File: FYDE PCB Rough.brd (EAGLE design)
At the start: 99 x 65.7 mm, 4 parts, among them P1 SEN-11574, U1 MCU-MCP3008-I/P(DIP16-7.62MM), X1 RASPI_BOARD_B+_FP

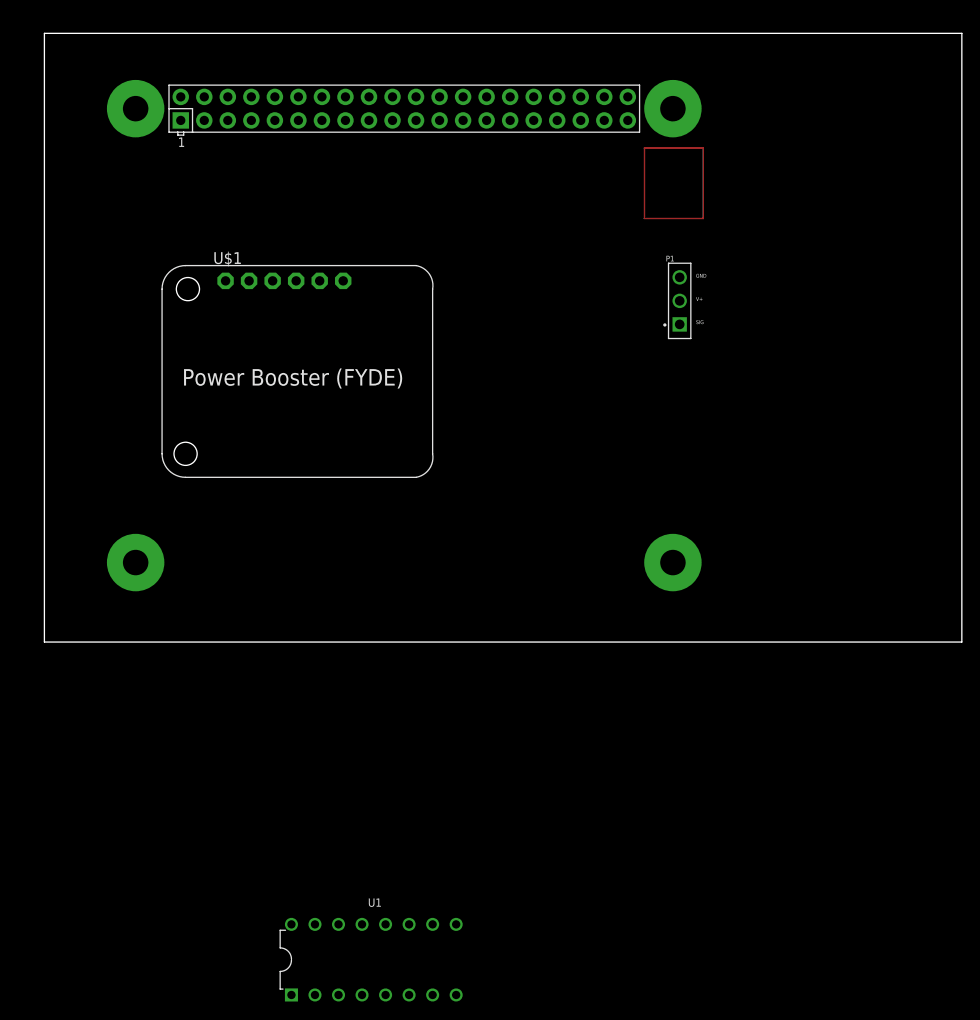
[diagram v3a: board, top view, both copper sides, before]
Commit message: schematic missing extra holes
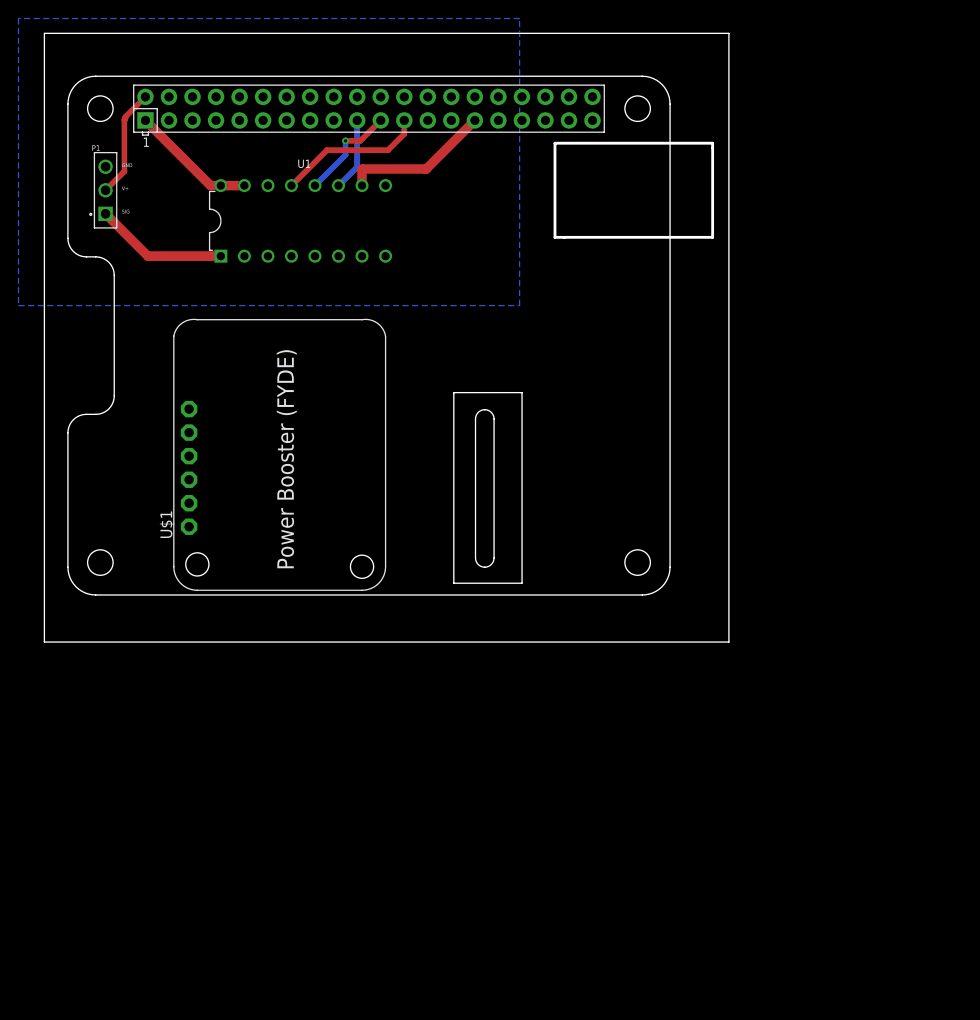
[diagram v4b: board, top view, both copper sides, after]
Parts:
- X1: value RASPI_BOARD_B+_FP -> RASPI_BOARD_B+_HDC; device raspberrypi_bastelstube_v13:RASPI_BOARD_B+_FULL_PAD -> raspberrypi_bastelstube_v13:RASPI_BOARD_B+HAT_DF_CF
- moved U1 80.1 mm to (27.9, 45.5)
- moved P1 63.1 mm to (6.60, 48.8)
- moved U$1 27.0 mm to (36.8, 5.59), turned to 90 degrees
- moved X1 3.81 mm to (2.54, 5.08)
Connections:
- removed net 3V3: X1.1
- removed net 5V0: X1.2
- removed net V+: P1.2
- new net +3V3A: U1.15, U1.16, X1.1
- new net +5V: P1.2, X1.2
- new net CLK: U1.13, X1.23
- new net CS: U1.10, X1.29
- new net MISO: U1.12, X1.21
- new net MOSI: U1.11, X1.19
- new net SIGNAL: P1.1, U1.1
- net GND: now also U1.14, U1.9
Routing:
- net N$7: track 27.9 -> 0.00 mm
- net CS: track 0.00 -> 16.1 mm
- net CLK: track 0.00 -> 15.9 mm
- net SIGNAL: track 0.00 -> 14.3 mm
- net +3V3A: track 0.00 -> 13.6 mm
- net +5V: track 0.00 -> 11.9 mm
- net MISO: track 0.00 -> 10.9 mm, vias 0 -> 1
- net MOSI: track 0.00 -> 7.87 mm
- added copper zone on layer 16, net GND
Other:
- board size 99 x 65.7 mm -> 73.9 x 65.7 mm
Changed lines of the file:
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@@
 <setting verticaltext="up"/>
 </settings>
-<grid distance="50" unitdist="mil" unit="mil" style="lines" multiple="1" display="no" altdistance="5" altunitdist="mil" altunit="mil"/>
+<grid distance="10" unitdist="mil" unit="mil" style="lines" multiple="1" display="no" altdistance="5" altunitdist="mil" altunit="mil"/>
 <layers>
 <layer number="1" name="Top" color="4" fill="1" visible="yes" active="yes"/>
@@
 <layer number="43" name="vRestrict" color="2" fill="10" visible="yes" active="yes"/>
 <layer number="44" name="Drills" color="7" fill="1" visible="no" active="yes"/>
-<layer number="45" name="Holes" color="7" fill="1" visible="no" active="yes"/>
+<layer number="45" name="Holes" color="7" fill="1" visible="yes" active="yes"/>
 <layer number="46" name="Milling" color="3" fill="1" visible="no" active="yes"/>
 <layer number="47" name="Measures" color="7" fill="1" visible="no" active="yes"/>
@@
 <board>
 <plain>
-<wire x1="0" y1="0" x2="99.04" y2="0" width="0" layer="20"/>
-<wire x1="99.04" y1="0" x2="99.04" y2="65.71" width="0" layer="20"/>
-<wire x1="99.04" y1="65.71" x2="0" y2="65.71" width="0" layer="20"/>
+<wire x1="0" y1="0" x2="73.894" y2="0" width="0" layer="20"/>
+<wire x1="73.894" y1="0" x2="73.894" y2="65.71" width="0" layer="20"/>
+<wire x1="73.894" y1="65.71" x2="0" y2="65.71" width="0" layer="20"/>
 <wire x1="0" y1="65.71" x2="0" y2="0" width="0" layer="20"/>
 <dimension x1="-16.129" y1="-139.7" x2="-9.906" y2="-116.967" x3="-29.083" y3="-128.3335" textsize="1.778" layer="47" dtype="vertical" unit="inch"/>
+<polygon width="0.3048" layer="20">
+<vertex x="55.118" y="53.848"/>
+<vertex x="72.136" y="53.848"/>
+<vertex x="72.136" y="53.34"/>
+<vertex x="72.136" y="43.688"/>
+<vertex x="56.134" y="43.688"/>
+<vertex x="55.118" y="43.688"/>
+</polygon>
+<rectangle x1="44.196" y1="6.35" x2="51.562" y2="26.924" layer="20"/>
 </plain>
 <attributes>
@@
 </autorouter>
 <elements>
-<element name="P1" library="SEN-11574" package="XDCR_SEN-11574" value="SEN-11574" x="68.58" y="36.83">
-<attribute name="AVAILABILITY" value="Unavailable" x="68.58" y="36.83" size="1.778" layer="27" display="off"/>
-<attribute name="DESCRIPTION" value=" PULSE SENSOR FOR ARDUINO " x="68.58" y="36.83" size="1.778" layer="27" display="off"/>
-<attribute name="MF" value="SparkFun" x="68.58" y="36.83" size="1.778" layer="27" display="off"/>
-<attribute name="MP" value="SEN-11574" x="68.58" y="36.83" size="1.778" layer="27" display="off"/>
-<attribute name="PACKAGE" value="None" x="68.58" y="36.83" size="1.778" layer="27" display="off"/>
-<attribute name="PRICE" value="None" x="68.58" y="36.83" size="1.778" layer="27" display="off"/>
+<element name="P1" library="SEN-11574" package="XDCR_SEN-11574" value="SEN-11574" x="6.604" y="48.768">
+<attribute name="AVAILABILITY" value="Unavailable" x="6.604" y="48.768" size="1.778" layer="27" display="off"/>
+<attribute name="DESCRIPTION" value=" PULSE SENSOR FOR ARDUINO " x="6.604" y="48.768" size="1.778" layer="27" display="off"/>
+<attribute name="MF" value="SparkFun" x="6.604" y="48.768" size="1.778" layer="27" display="off"/>
+<attribute name="MP" value="SEN-11574" x="6.604" y="48.768" size="1.778" layer="27" display="off"/>
+<attribute name="PACKAGE" value="None" x="6.604" y="48.768" size="1.778" layer="27" display="off"/>
+<attribute name="PRICE" value="None" x="6.604" y="48.768" size="1.778" layer="27" display="off"/>
 </element>
-<element name="X1" library="raspberrypi_bastelstube_v13" package="RASPI_BOARD_B+_FULL_PAD" value="RASPI_BOARD_B+_FP" x="6.35" y="5.08"/>
-<element name="U$1" library="Adafruit-PowerBoost-FYDE" package="ADAFRUITPOWERBOOSTER(FYDE)" value="ADAFRUITPOWERBOOSTER(FYDE)" x="12.7" y="17.78"/>
-<element name="U1" library="MCU-MCP3008-I_P_DIP16-7.62MM_" package="DIP16-2.54-19.2X7.62MM" value="MCU-MCP3008-I/P(DIP16-7.62MM)" x="35.56" y="-34.29">
-<attribute name="AVAILABILITY" value="Unavailable" x="35.56" y="-34.29" size="1.778" layer="27" display="off"/>
-<attribute name="DESCRIPTION" value=" 10 Bit Analog to Digital Converter 4, 8 Input 1 SAR 16-PDIP " x="35.56" y="-34.29" size="1.778" layer="27" display="off"/>
-<attribute name="MF" value="Microchip" x="35.56" y="-34.29" size="1.778" layer="27" display="off"/>
-<attribute name="MP" value="MCP3008-I/P" x="35.56" y="-34.29" size="1.778" layer="27" display="off"/>
-<attribute name="PACKAGE" value="DIP-16 Microchip" x="35.56" y="-34.29" size="1.778" layer="27" display="off"/>
-<attribute name="PRICE" value="None" x="35.56" y="-34.29" size="1.778" layer="27" display="off"/>
+<element name="U$1" library="Adafruit-PowerBoost-FYDE" package="ADAFRUITPOWERBOOSTER(FYDE)" value="ADAFRUITPOWERBOOSTER(FYDE)" x="36.83" y="5.588" rot="R90"/>
+<element name="U1" library="MCU-MCP3008-I_P_DIP16-7.62MM_" package="DIP16-2.54-19.2X7.62MM" value="MCU-MCP3008-I/P(DIP16-7.62MM)" x="27.94" y="45.466">
+<attribute name="AVAILABILITY" value="Unavailable" x="27.94" y="45.466" size="1.778" layer="27" display="off"/>
+<attribute name="DESCRIPTION" value=" 10 Bit Analog to Digital Converter 4, 8 Input 1 SAR 16-PDIP " x="27.94" y="45.466" size="1.778" layer="27" display="off"/>
+<attribute name="MF" value="Microchip" x="27.94" y="45.466" size="1.778" layer="27" display="off"/>
+<attribute name="MP" value="MCP3008-I/P" x="27.94" y="45.466" size="1.778" layer="27" display="off"/>
+<attribute name="PACKAGE" value="DIP-16 Microchip" x="27.94" y="45.466" size="1.778" layer="27" display="off"/>
+<attribute name="PRICE" value="None" x="27.94" y="45.466" size="1.778" layer="27" display="off"/>
 </element>
+<element name="X1" library="raspberrypi_bastelstube_v13" package="RASPI_BOARD_B+HAT_DF_CF" value="RASPI_BOARD_B+_HDC" x="2.54" y="5.08"/>
 </elements>
 <signals>
-<signal name="V+">
-<contactref element="P1" pad="2"/>
-</signal>
 <signal name="GND">
 <contactref element="P1" pad="3"/>
+<contactref element="U1" pad="14"/>
+<contactref element="U1" pad="9"/>
 <contactref element="X1" pad="6"/>
-<wire x1="19.8" y1="58.85" x2="68.58" y2="39.37" width="0" layer="19" extent="1-1"/>
-</signal>
-<signal name="5V0">
+<polygon width="0.3048" layer="16">
+<vertex x="-2.794" y="67.31"/>
+<vertex x="-2.794" y="36.322"/>
+<vertex x="51.308" y="36.322"/>
+<vertex x="51.308" y="67.31"/>
+</polygon>
+</signal>
+<signal name="+3V3A">
+<contactref element="U1" pad="16"/>
+<contactref element="U1" pad="15"/>
+<contactref element="X1" pad="1"/>
+<wire x1="10.91" y1="56.31" x2="17.944" y2="49.276" width="1.016" layer="1"/>
+<wire x1="17.944" y1="49.276" x2="19.05" y2="49.276" width="1.016" layer="1"/>
+<wire x1="19.05" y1="49.276" x2="21.59" y2="49.276" width="1.016" layer="1"/>
+</signal>
+<signal name="CLK">
+<contactref element="U1" pad="13"/>
+<contactref element="X1" pad="23"/>
+<wire x1="26.67" y1="49.276" x2="30.48" y2="53.086" width="0.6096" layer="1"/>
+<wire x1="30.48" y1="53.086" x2="37.084" y2="53.086" width="0.6096" layer="1"/>
+<wire x1="37.084" y1="53.086" x2="38.85" y2="54.852" width="0.6096" layer="1"/>
+<wire x1="38.85" y1="54.852" x2="38.85" y2="56.31" width="0.6096" layer="1"/>
+</signal>
+<signal name="MISO">
+<contactref element="U1" pad="12"/>
+<contactref element="X1" pad="21"/>
+<wire x1="29.21" y1="49.276" x2="32.512" y2="52.578" width="0.6096" layer="16"/>
+<wire x1="32.512" y1="52.578" x2="32.512" y2="54.102" width="0.6096" layer="16"/>
+<via x="32.512" y="54.102" extent="1-16" drill="0.35"/>
+<wire x1="32.512" y1="54.102" x2="34.102" y2="54.102" width="0.6096" layer="1"/>
+<wire x1="34.102" y1="54.102" x2="36.31" y2="56.31" width="0.6096" layer="1"/>
+</signal>
+<signal name="MOSI">
+<contactref element="U1" pad="11"/>
+<contactref element="X1" pad="19"/>
+<wire x1="33.77" y1="56.31" x2="33.77" y2="51.296" width="0.6096" layer="16"/>
+<wire x1="33.77" y1="51.296" x2="31.75" y2="49.276" width="0.6096" layer="16"/>
+</signal>
+<signal name="SIGNAL">
+<contactref element="U1" pad="1"/>
+<contactref element="P1" pad="1"/>
+<wire x1="6.604" y1="46.228" x2="11.176" y2="41.656" width="1.016" layer="1"/>
+<wire x1="11.176" y1="41.656" x2="19.05" y2="41.656" width="1.016" layer="1"/>
+</signal>
+<signal name="+5V">
+<contactref element="P1" pad="2"/>
 <contactref element="X1" pad="2"/>
-</signal>
-<signal name="3V3">
-<contactref element="X1" pad="1"/>
-</signal>
-<signal name="N$7">
-<wire x1="64.77" y1="53.34" x2="71.12" y2="53.34" width="0.1524" layer="1"/>
-<wire x1="71.12" y1="53.34" x2="71.12" y2="45.72" width="0.1524" layer="1"/>
-<wire x1="71.12" y1="45.72" x2="64.77" y2="45.72" width="0.1524" layer="1"/>
-<wire x1="64.77" y1="53.34" x2="64.77" y2="45.72" width="0.1524" layer="1"/>
+<wire x1="6.604" y1="48.768" x2="8.636" y2="50.8" width="0.6096" layer="1"/>
+<wire x1="8.636" y1="56.3635625" x2="8.7358" y2="56.4633625" width="0.6096" layer="1"/>
+<wire x1="8.7358" y1="56.4633625" x2="8.7358" y2="56.6758" width="0.6096" layer="1"/>
+<wire x1="8.7358" y1="56.6758" x2="10.91" y2="58.85" width="0.6096" layer="1"/>
+<wire x1="8.636" y1="50.8" x2="8.636" y2="56.3635625" width="0.6096" layer="1"/>
+</signal>
+<signal name="CS">
+<contactref element="X1" pad="29"/>
+<contactref element="U1" pad="10"/>
+<wire x1="46.47" y1="56.31" x2="41.214" y2="51.054" width="1.016" layer="1"/>
+<wire x1="41.214" y1="51.054" x2="34.29" y2="51.054" width="1.016" layer="1"/>
+<wire x1="34.29" y1="51.054" x2="34.29" y2="49.276" width="1.016" layer="1"/>
 </signal>
 </signals>

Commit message: Add files via upload
now with holes!
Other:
- board size 73.9 x 65.7 mm -> 65 x 56.1 mm
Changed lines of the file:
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@@
 <board>
 <plain>
-<wire x1="0" y1="0" x2="73.894" y2="0" width="0" layer="20"/>
-<wire x1="73.894" y1="0" x2="73.894" y2="65.71" width="0" layer="20"/>
-<wire x1="73.894" y1="65.71" x2="0" y2="65.71" width="0" layer="20"/>
-<wire x1="0" y1="65.71" x2="0" y2="0" width="0" layer="20"/>
 <dimension x1="-16.129" y1="-139.7" x2="-9.906" y2="-116.967" x3="-29.083" y3="-128.3335" textsize="1.778" layer="47" dtype="vertical" unit="inch"/>
-<polygon width="0.3048" layer="20">
-<vertex x="55.118" y="53.848"/>
-<vertex x="72.136" y="53.848"/>
-<vertex x="72.136" y="53.34"/>
-<vertex x="72.136" y="43.688"/>
-<vertex x="56.134" y="43.688"/>
-<vertex x="55.118" y="43.688"/>
-</polygon>
-<rectangle x1="44.196" y1="6.35" x2="51.562" y2="26.924" layer="20"/>
+<wire x1="2.54" y1="58.166" x2="5.588" y2="61.214" width="0.1524" layer="20" curve="-90"/>
+<wire x1="5.588" y1="61.214" x2="64.262" y2="61.214" width="0.1524" layer="20"/>
+<wire x1="64.262" y1="61.214" x2="67.564" y2="57.912" width="0.1524" layer="20" curve="-90"/>
+<wire x1="67.564" y1="57.912" x2="67.564" y2="54.102" width="0.1524" layer="20"/>
+<wire x1="67.564" y1="54.102" x2="67.31" y2="53.848" width="0.1524" layer="20" curve="-90"/>
+<wire x1="67.31" y1="53.848" x2="55.372" y2="53.848" width="0.1524" layer="20"/>
+<wire x1="55.372" y1="53.848" x2="55.118" y2="53.594" width="0.1524" layer="20" curve="90"/>
+<wire x1="55.118" y1="53.594" x2="55.118" y2="43.942" width="0.1524" layer="20"/>
+<wire x1="55.118" y1="43.942" x2="55.372" y2="43.688" width="0.1524" layer="20" curve="90"/>
+<wire x1="55.372" y1="43.688" x2="67.056" y2="43.688" width="0.1524" layer="20"/>
+<wire x1="67.056" y1="43.688" x2="67.564" y2="43.18" width="0.1524" layer="20" curve="-90"/>
+<wire x1="67.564" y1="43.18" x2="67.564" y2="8.382" width="0.1524" layer="20"/>
+<wire x1="67.564" y1="8.382" x2="64.262" y2="5.08" width="0.1524" layer="20" curve="-90"/>
+<wire x1="64.262" y1="5.08" x2="5.334" y2="5.08" width="0.1524" layer="20"/>
+<wire x1="5.334" y1="5.08" x2="2.54" y2="7.874" width="0.1524" layer="20" curve="-90"/>
+<wire x1="2.54" y1="7.874" x2="2.54" y2="22.606" width="0.1524" layer="20"/>
+<wire x1="2.54" y1="22.606" x2="4.572" y2="24.638" width="0.1524" layer="20" curve="-90"/>
+<wire x1="4.572" y1="24.638" x2="5.334" y2="24.638" width="0.1524" layer="20"/>
+<wire x1="5.334" y1="24.638" x2="7.366" y2="26.67" width="0.1524" layer="20" curve="90"/>
+<wire x1="7.366" y1="26.67" x2="7.366" y2="39.878" width="0.1524" layer="20"/>
+<wire x1="7.366" y1="39.878" x2="5.588" y2="41.656" width="0.1524" layer="20" curve="90"/>
+<wire x1="5.588" y1="41.656" x2="4.318" y2="41.656" width="0.1524" layer="20"/>
+<wire x1="4.318" y1="41.656" x2="2.54" y2="43.434" width="0.1524" layer="20" curve="-90"/>
+<wire x1="2.54" y1="43.434" x2="2.54" y2="58.166" width="0.1524" layer="20"/>
+<wire x1="44.196" y1="8.636" x2="44.196" y2="25.908" width="0.1524" layer="20"/>
+<wire x1="44.196" y1="25.908" x2="45.72" y2="27.432" width="0.1524" layer="20" curve="-90"/>
+<wire x1="45.72" y1="27.432" x2="50.8" y2="27.432" width="0.1524" layer="20"/>
+<wire x1="50.8" y1="27.432" x2="52.07" y2="26.162" width="0.1524" layer="20" curve="-90"/>
+<wire x1="52.07" y1="26.162" x2="52.07" y2="7.62" width="0.1524" layer="20"/>
+<wire x1="52.07" y1="7.62" x2="50.546" y2="6.096" width="0.1524" layer="20" curve="-90"/>
+<wire x1="50.546" y1="6.096" x2="45.466" y2="6.096" width="0.1524" layer="20"/>
+<wire x1="45.466" y1="6.096" x2="44.196" y2="7.366" width="0.1524" layer="20" curve="-90"/>
+<wire x1="44.196" y1="7.366" x2="44.196" y2="8.636" width="0.1524" layer="20"/>
 </plain>
 <attributes>
